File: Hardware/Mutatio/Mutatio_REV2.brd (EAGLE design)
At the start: 47.2 x 50 mm, 39 parts, among them IC1 DS3231/SO, IC2 74AUC1G14DBV, J1 MICRO-SDCARD-CONNECTOR-330006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

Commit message: finished revision 2
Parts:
- removed C11: 100uF, resistor:C1206
- added D6: (no value), diode:MINIMELF
- moved R4 1.14 mm to (9.10, 27.4)
- moved R5 1.12 mm to (11.3, 27.4)
- moved R6 1.10 mm to (6.80, 27.4)
- moved C10 0.32 mm to (1.70, 28.5), turned to 270 degrees
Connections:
- new net N$6: C10.1, D6.C, IC1.14
- net +3V3: no longer C10.1, C11.1, IC1.14
- net +5V: now also D6.A
- net GND: no longer C11.2
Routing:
- net WS2812_DATA: track 0.00 -> 53.9 mm, vias 0 -> 2
- net SCL: track 69.5 -> 86.3 mm
- net +5V: track 105.4 -> 121.2 mm
- net +3V3: track 439.6 -> 454.1 mm
- net SDA: track 62.0 -> 73.6 mm
- net !SDCARD_DETECT: track 33.5 -> 43.5 mm, vias 1 -> 3
- net N$6: track 0.00 -> 9.27 mm
- net GND: track 31.8 -> 39.0 mm
- net SIGNAL: track 53.5 -> 60.4 mm
- net VDD: track 24.1 -> 30.2 mm
- net BOARDANTENNA: track 449.8 -> 454.7 mm
- net SPI_MISO: track 19.7 -> 24.0 mm
- net SD_CSN: track 41.7 -> 46.0 mm
- net N$3: track 2.98 -> 5.84 mm
- net SPI_MOSI: track 15.4 -> 17.3 mm
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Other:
- board text added: "22. MAR. 2016"
- board text added: "REV2"
- board text added: "REVISION 2"
- board text removed: "17. JAN. 2016"
- board text removed: "REVISION 1"

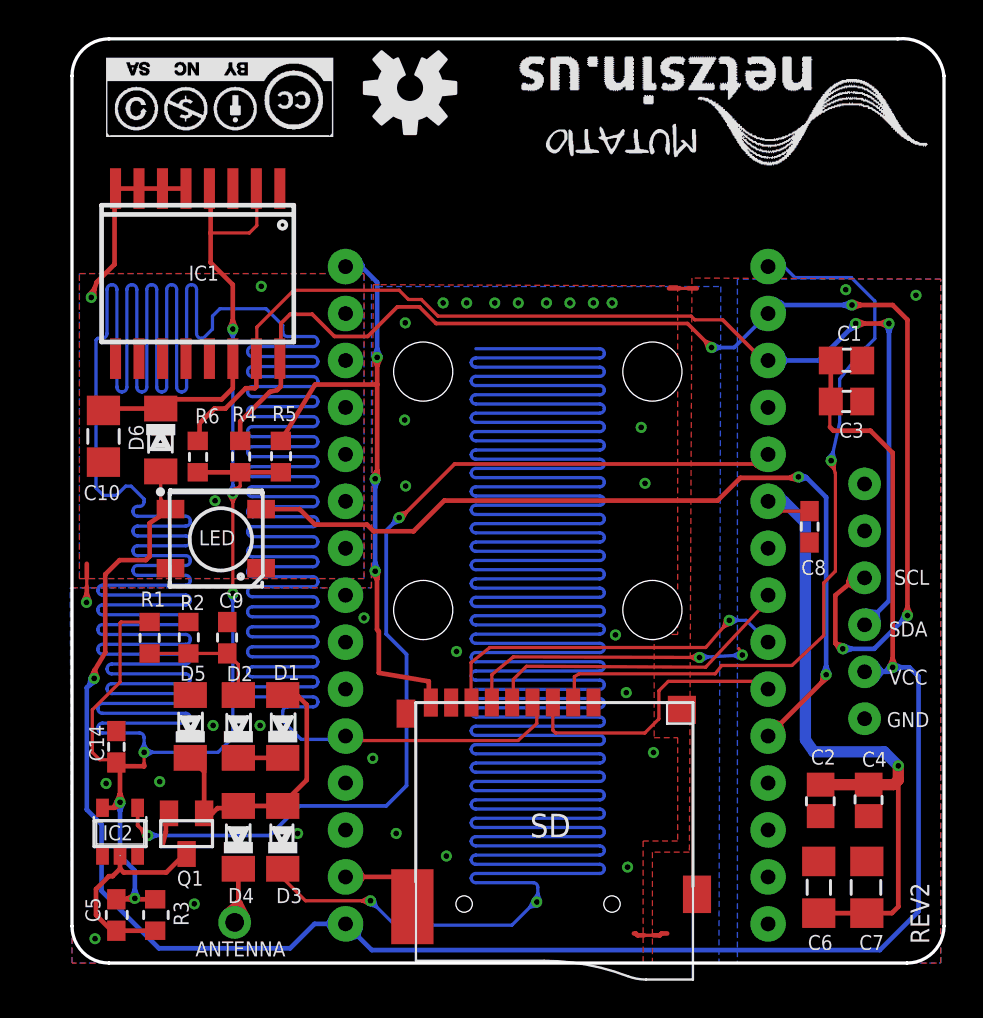
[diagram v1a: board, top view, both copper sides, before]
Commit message: Updated REV2 hardware
changed the Signal and the LED pin so upload and bootup works properly
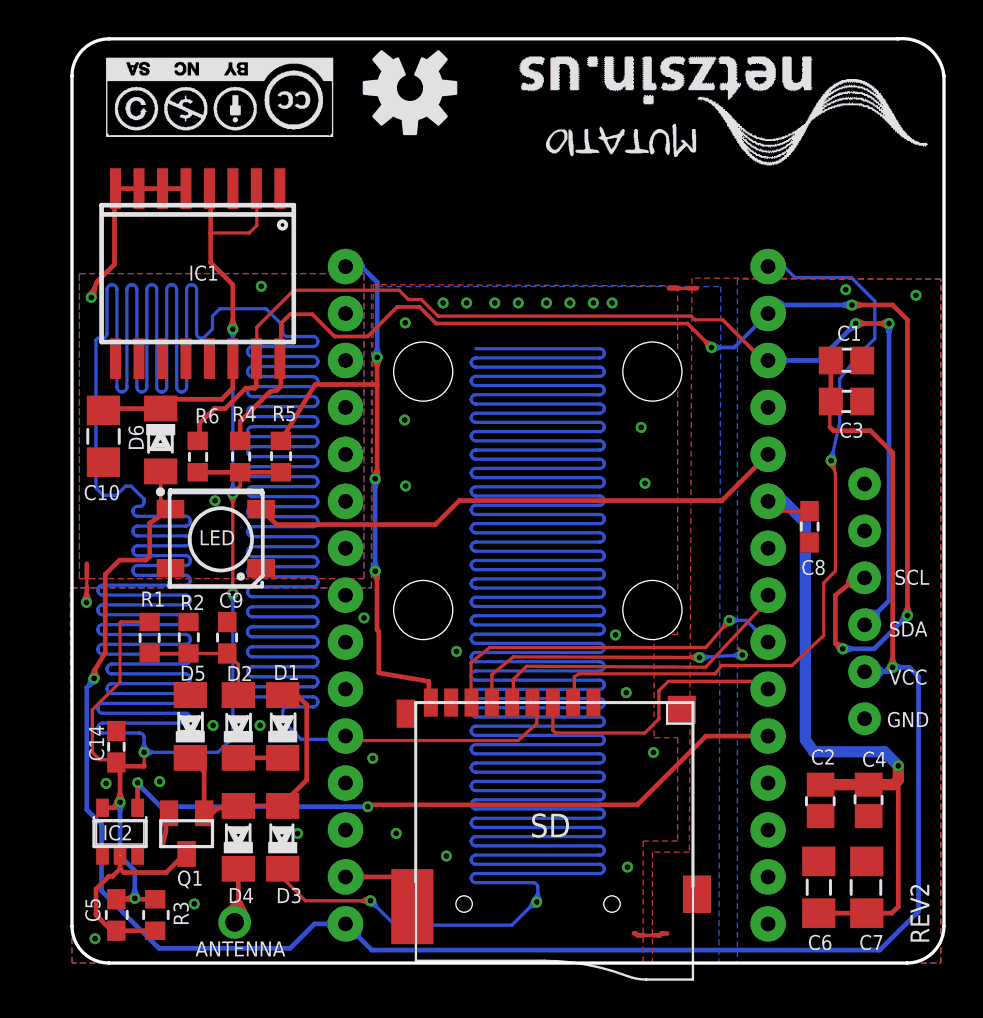
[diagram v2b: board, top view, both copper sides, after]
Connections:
- net SIGNAL: now also U$2.D8; no longer U$2.D4
- net WS2812_DATA: now also U$2.D4; no longer U$2.D8
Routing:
- net WS2812_DATA: track 53.9 -> 29.3 mm, vias 2 -> 0
- net SIGNAL: track 60.4 -> 37.6 mm
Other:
- board text added: "DAMIAN SCHNEIDER, WINTERTHUR"
- board text removed: "DAMIAN SCHNEIDER, WINTERTHR"
